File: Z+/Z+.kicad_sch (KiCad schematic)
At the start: 30 parts, among them J1 200528-0100

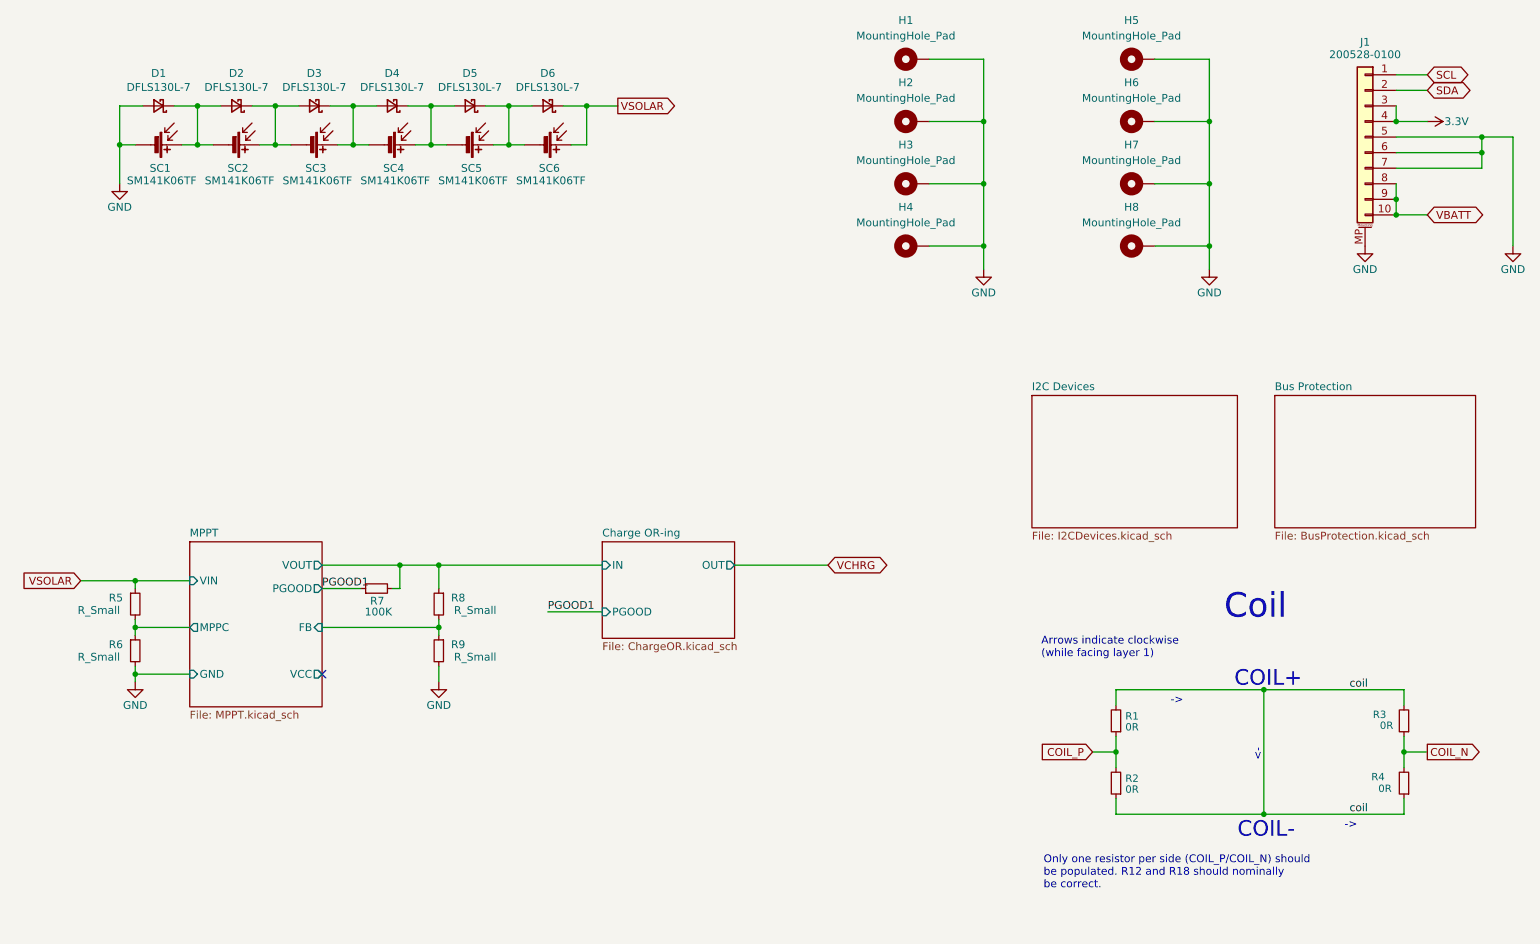
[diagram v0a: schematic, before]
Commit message: Added DRV8235, Quad Light Sensor, and refactored schematics
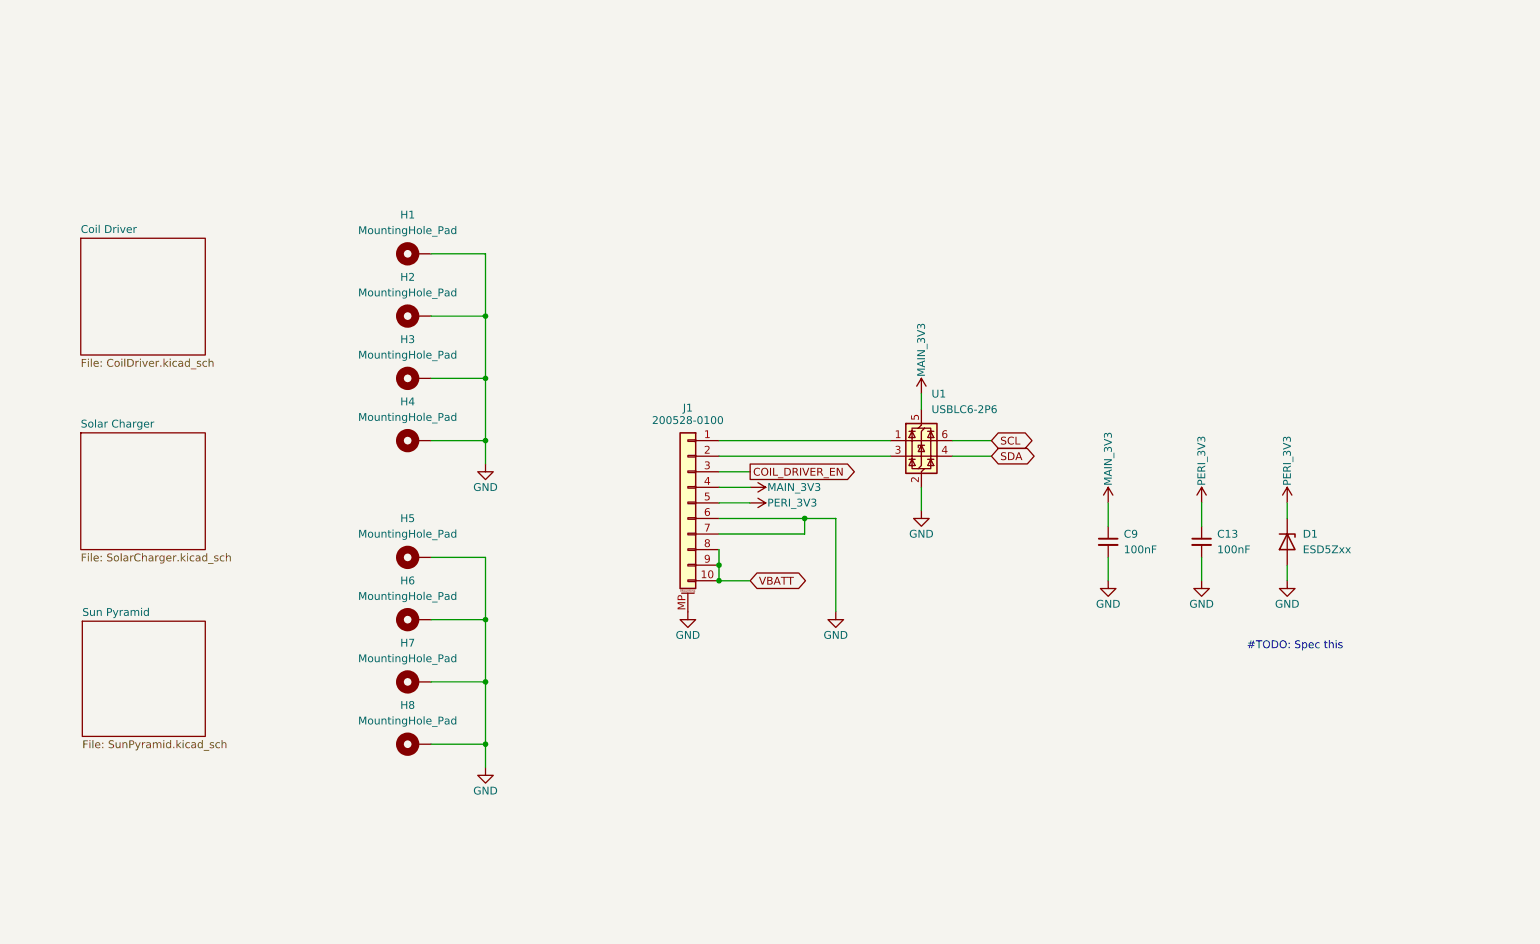
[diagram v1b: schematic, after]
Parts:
- removed D1, D2, D3, D4, D5, D6: DFLS130L-7, Diode_SMD:D_PowerDI-123, symbol Device:D_Schottky_Small
- removed R1, R2, R3, R4: 0R, Resistor_SMD:R_0603_1608Metric, symbol Device:R_Small
- removed R5, R6, R8, R9: R_Small, Resistor_SMD:R_0603_1608Metric, symbol Device:R_Small
- removed R7: 100K, Resistor_SMD:R_0603_1608Metric, symbol Device:R_Small
- removed SC1, SC2, SC3, SC4, SC5, SC6: SM141K06TF, SolarPanels:SM141K06TF, symbol Device:Solar_Cell
- added C13, C9: 100nF, Capacitor_SMD:C_0603_1608Metric, symbol Device:C_Small
- added D1: ESD5Zxx, Diode_SMD:D_SOD-523, symbol Diode:ESD5Zxx
- added U1: USBLC6-2P6, Package_TO_SOT_SMD:SOT-666, symbol Power_Protection:USBLC6-2P6
- J1: footprint Connector_FFC-FPC:Molex_200528-0100_1x10-1MP_P1.00mm_Horizontal -> Argus-Connectors:Molex_200528-0100_1x10-1MP_P1.00mm_Horizontal
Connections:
- net GND: now also C13.2, C9.2, D1.2 (A), U1.2 (GND); no longer J1.5 (Pin_5)
- net SCL: now also U1.6 (I/O1); no longer J1.1 (Pin_1)
- net SDA: now also U1.4 (I/O2); no longer J1.2 (Pin_2)
- net 3.3V renamed COIL_DRIVER_EN
- net COIL_DRIVER_EN: no longer J1.4 (Pin_4)
- new net: J1.1 (Pin_1), U1.1 (I/O1)
- new net: J1.2 (Pin_2), U1.3 (I/O2)
- new net MAIN_3V3: C9.1, J1.4 (Pin_4), U1.5 (VBUS)
- new net PERI_3V3: C13.1, D1.1 (K), J1.5 (Pin_5)
- no-connect marks 1 -> 0
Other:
- sheet I2C Devices renamed Sun Pyramid
- removed sheet Bus Protection
- removed sheet Charge OR-ing
- removed sheet MPPT
- added sheet Coil Driver (CoilDriver.kicad_sch)
- added sheet Solar Charger (SolarCharger.kicad_sch)
- sheet Sun Pyramid: file I2CDevices.kicad_sch -> SunPyramid.kicad_sch
- note added: "#TODO: Spec this"
- note removed: "->"
- note removed: "<-"
- note removed: "Arrows indicate clockwise (while facing layer 1)"
- note removed: "COIL+"
- note removed: "COIL-"
- note removed: "Coil"
- note removed: "Only one resistor per side (COIL_P/COIL_N) should be populated. R12 and R18 should nominally be correct."
- moved on the sheet: H1, H2, H3, H4, H5, H6, H7, H8

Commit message: Z+ updates WIP
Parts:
- H1, H2, H3, H4, H5, H6, H7, H8: footprint SolarPanels:MountingHole_3.2mm_M3_DIN965_Pad_TopBottom -> Argus-Miscellaneous:MountingHole_3.2mm_M3_DIN965_Pad_TopBottom
- renumbered C9 to C1, C13 to C2
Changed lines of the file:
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@@
 			)
 		)
-		(property "Footprint" "SolarPanels:MountingHole_3.2mm_M3_DIN965_Pad_TopBottom"
+		(property "Footprint" "Argus-Miscellaneous:MountingHole_3.2mm_M3_DIN965_Pad_TopBottom"
 			(at 95.25 135.89 0)
 			(effects
@@
 		(on_board yes)
 		(dnp no)
-		(property "Reference" "#PWR09"
+		(property "Reference" "#PWR08"
 			(at 237.49 115.57 0)
 			(effects
@@
 			(project "Z+"
 				(path "/977a45af-b6d4-4b54-8e70-e74e2c44e8e7"
-					(reference "#PWR09")
+					(reference "#PWR08")
 					(unit 1)
 				)
@@
 			)
 		)
-		(property "Footprint" "SolarPanels:MountingHole_3.2mm_M3_DIN965_Pad_TopBottom"
+		(property "Footprint" "Argus-Miscellaneous:MountingHole_3.2mm_M3_DIN965_Pad_TopBottom"
 			(at 95.25 76.2 0)
 			(effects
@@
 		(dnp no)
 		(fields_autoplaced yes)
-		(property "Reference" "C9"
+		(property "Reference" "C1"
 			(at 210.82 101.6062 0)
 			(effects
@@
 			(project "Z+"
 				(path "/977a45af-b6d4-4b54-8e70-e74e2c44e8e7"
-					(reference "C9")
+					(reference "C1")
 					(unit 1)
 				)
@@
 		(on_board yes)
 		(dnp no)
-		(property "Reference" "#PWR01"
+		(property "Reference" "#PWR03"
 			(at 139.7 120.65 0)
 			(effects
@@
 			(project "Z+"
 				(path "/977a45af-b6d4-4b54-8e70-e74e2c44e8e7"
-					(reference "#PWR01")
+					(reference "#PWR03")
 					(unit 1)
 				)
@@
 		(on_board yes)
 		(dnp no)
-		(property "Reference" "#PWR03"
+		(property "Reference" "#PWR04"
 			(at 163.83 120.65 0)
 			(effects
@@
 			(project "Z+"
 				(path "/977a45af-b6d4-4b54-8e70-e74e2c44e8e7"
-					(reference "#PWR03")
+					(reference "#PWR04")
 					(unit 1)
 				)
@@
 		(on_board yes)
 		(dnp no)
-		(property "Reference" "#PWR02"
+		(property "Reference" "#PWR01"
 			(at 106.68 96.52 0)
 			(effects
@@
 			(project "Z+"
 				(path "/977a45af-b6d4-4b54-8e70-e74e2c44e8e7"
-					(reference "#PWR02")
+					(reference "#PWR01")
 					(unit 1)
 				)
@@
 		(on_board yes)
 		(dnp no)
-		(property "Reference" "#SUPPLY023"
+		(property "Reference" "#SUPPLY03"
 			(at 177.8 78.74 0)
 			(effects
@@
 			(project "Z+"
 				(path "/977a45af-b6d4-4b54-8e70-e74e2c44e8e7"
-					(reference "#SUPPLY023")
+					(reference "#SUPPLY03")
 					(unit 1)
 				)
@@
 		(on_board yes)
 		(dnp no)
-		(property "Reference" "#SUPPLY02"
+		(property "Reference" "#SUPPLY06"
 			(at 237.49 96.52 0)
 			(effects
@@
 			(project "Z+"
 				(path "/977a45af-b6d4-4b54-8e70-e74e2c44e8e7"
-					(reference "#SUPPLY02")
+					(reference "#SUPPLY06")
 					(unit 1)
 				)
@@
 			)
 		)
-		(property "Footprint" "SolarPanels:MountingHole_3.2mm_M3_DIN965_Pad_TopBottom"
+		(property "Footprint" "Argus-Miscellaneous:MountingHole_3.2mm_M3_DIN965_Pad_TopBottom"
 			(at 95.25 125.73 0)
 			(effects
@@
 			)
 		)
-		(property "Footprint" "SolarPanels:MountingHole_3.2mm_M3_DIN965_Pad_TopBottom"
+		(property "Footprint" "Argus-Miscellaneous:MountingHole_3.2mm_M3_DIN965_Pad_TopBottom"
 			(at 95.25 115.57 0)
 			(effects
@@
 		(on_board yes)
 		(dnp no)
-		(property "Reference" "#PWR034"
+		(property "Reference" "#PWR02"
 			(at 106.68 146.05 0)
 			(effects
@@
 			(project "Z+"
 				(path "/977a45af-b6d4-4b54-8e70-e74e2c44e8e7"
-					(reference "#PWR034")
+					(reference "#PWR02")
 					(unit 1)
 				)
@@
 		(on_board yes)
 		(dnp no)
-		(property "Reference" "#PWR04"
+		(property "Reference" "#PWR05"
 			(at 177.8 104.14 0)
 			(effects
@@
 			(project "Z+"
 				(path "/977a45af-b6d4-4b54-8e70-e74e2c44e8e7"
-					(reference "#PWR04")
+					(reference "#PWR05")
 					(unit 1)
 				)
@@
 		(on_board yes)
 		(dnp no)
-		(property "Reference" "#PWR05"
+		(property "Reference" "#PWR06"
 			(at 208.28 115.57 0)
 			(effects
@@
 			(project "Z+"
 				(path "/977a45af-b6d4-4b54-8e70-e74e2c44e8e7"
-					(reference "#PWR05")
+					(reference "#PWR06")
 					(unit 1)
 				)
@@
 			)
 		)
-		(property "Footprint" "SolarPanels:MountingHole_3.2mm_M3_DIN965_Pad_TopBottom"
+		(property "Footprint" "Argus-Miscellaneous:MountingHole_3.2mm_M3_DIN965_Pad_TopBottom"
 			(at 95.25 86.36 0)
 			(effects
@@
 			)
 		)
-		(property "Footprint" "SolarPanels:MountingHole_3.2mm_M3_DIN965_Pad_TopBottom"
+		(property "Footprint" "Argus-Miscellaneous:MountingHole_3.2mm_M3_DIN965_Pad_TopBottom"
 			(at 95.25 66.04 0)
 			(effects
@@
 		(on_board yes)
 		(dnp no)
-		(property "Reference" "#SUPPLY025"
+		(property "Reference" "#SUPPLY05"
 			(at 223.52 96.52 0)
 			(effects
@@
 			(project "Z+"
 				(path "/977a45af-b6d4-4b54-8e70-e74e2c44e8e7"
-					(reference "#SUPPLY025")
+					(reference "#SUPPLY05")
 					(unit 1)
 				)
@@
 		(on_board yes)
 		(dnp no)
-		(property "Reference" "#SUPPLY024"
+		(property "Reference" "#SUPPLY04"
 			(at 208.28 96.52 0)
 			(effects
@@
 			(project "Z+"
 				(path "/977a45af-b6d4-4b54-8e70-e74e2c44e8e7"
-					(reference "#SUPPLY024")
+					(reference "#SUPPLY04")
 					(unit 1)
 				)
@@
 			)
 		)
-		(property "Footprint" "SolarPanels:MountingHole_3.2mm_M3_DIN965_Pad_TopBottom"
+		(property "Footprint" "Argus-Miscellaneous:MountingHole_3.2mm_M3_DIN965_Pad_TopBottom"
 			(at 95.25 105.41 0)
 			(effects
@@
 		(dnp no)
 		(fields_autoplaced yes)
-		(property "Reference" "C13"
+		(property "Reference" "C2"
 			(at 226.06 101.6062 0)
 			(effects
@@
 			(project "Z+"
 				(path "/977a45af-b6d4-4b54-8e70-e74e2c44e8e7"
-					(reference "C13")
+					(reference "C2")
 					(unit 1)
 				)
@@
 		(on_board yes)
 		(dnp no)
-		(property "Reference" "#PWR06"
+		(property "Reference" "#PWR07"
 			(at 223.52 115.57 0)
 			(effects
@@
 			(project "Z+"
 				(path "/977a45af-b6d4-4b54-8e70-e74e2c44e8e7"
-					(reference "#PWR06")
+					(reference "#PWR07")
 					(unit 1)
 				)
@@
 			)
 		)
-		(property "Footprint" "SolarPanels:MountingHole_3.2mm_M3_DIN965_Pad_TopBottom"
+		(property "Footprint" "Argus-Miscellaneous:MountingHole_3.2mm_M3_DIN965_Pad_TopBottom"
 			(at 95.25 55.88 0)
 			(effects
@@
 		(on_board yes)
 		(dnp no)
-		(property "Reference" "#SUPPLY022"
+		(property "Reference" "#SUPPLY02"
 			(at 149.86 96.52 0)
 			(effects
@@
 			(project "Z+"
 				(path "/977a45af-b6d4-4b54-8e70-e74e2c44e8e7"
-					(reference "#SUPPLY022")
-					(unit 1)
-				)
+					(reference "#SUPPLY02")
+					(unit 1)
+				)

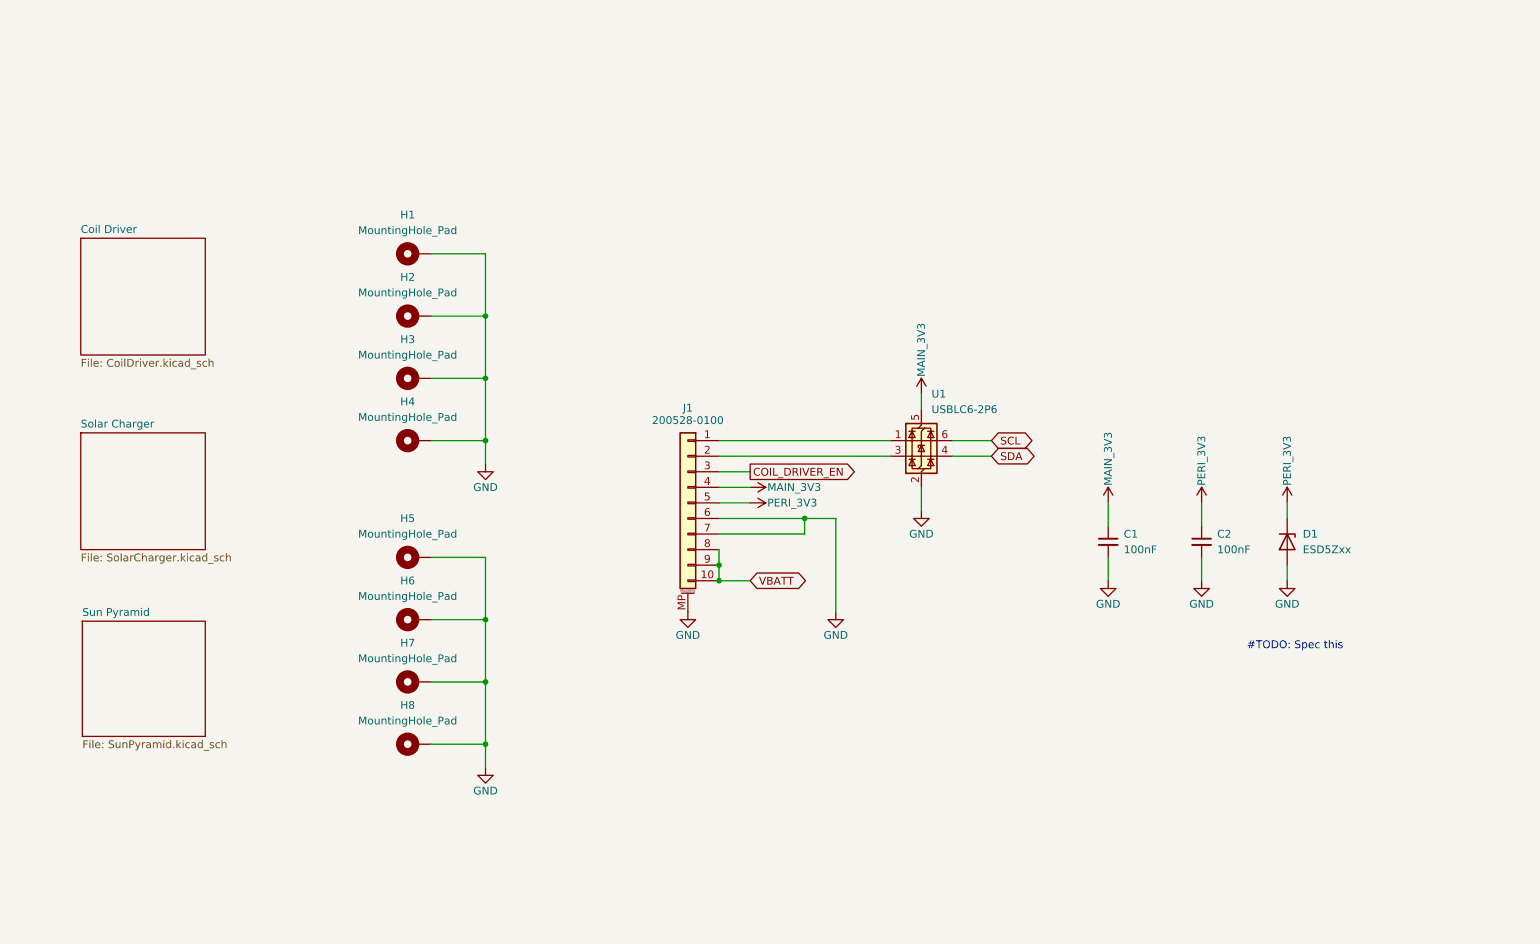
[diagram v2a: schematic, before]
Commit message: Placed all components
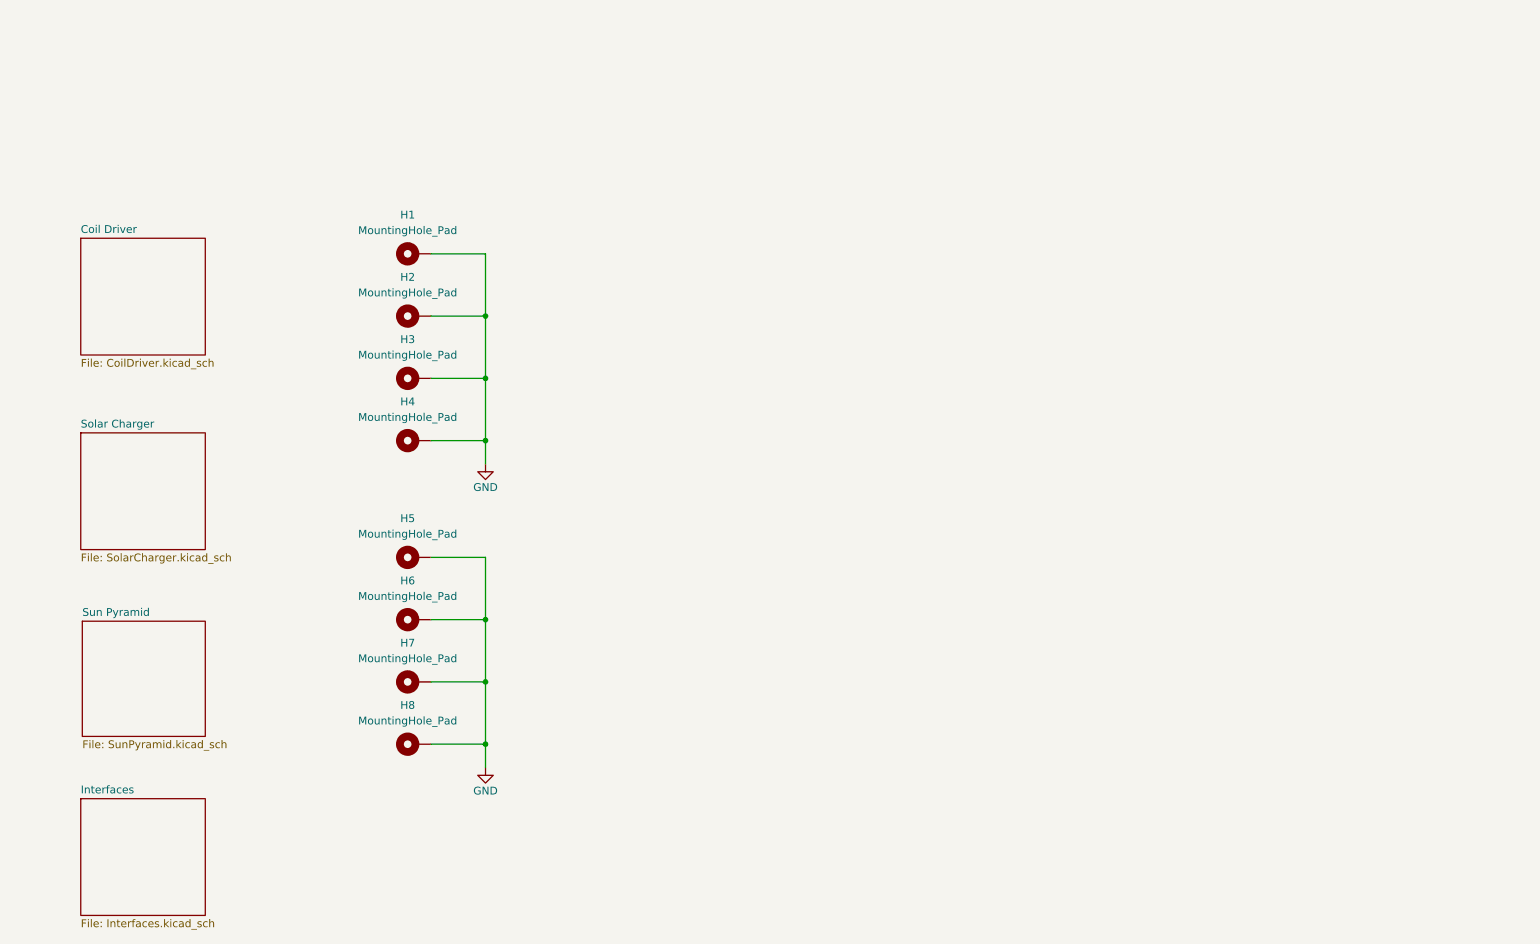
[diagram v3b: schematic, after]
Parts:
- removed C1, C2: 100nF, Capacitor_SMD:C_0603_1608Metric, symbol Device:C_Small
- removed D1: ESD5Zxx, Diode_SMD:D_SOD-523, symbol Diode:ESD5Zxx
- removed J1: 200528-0100, Argus-Connectors:Molex_200528-0100_1x10-1MP_P1.00mm_Horizontal, symbol Connector_Generic_MountingPin:Conn_01x10_MountingPin
- removed U1: USBLC6-2P6, Package_TO_SOT_SMD:SOT-666, symbol Power_Protection:USBLC6-2P6
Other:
- added sheet Interfaces (Interfaces.kicad_sch)
- note removed: "#TODO: Spec this"

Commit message: More layout work
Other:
- moved on the sheet: H1, H2, H3, H4, H5, H6, H7, H8
